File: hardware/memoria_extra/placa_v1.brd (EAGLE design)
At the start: 37.1 x 30.4 mm, 10 parts, among them IC1 CY7C1049CV33T, IC2 REG1117, J10 M14, J11 M14, J9 M14

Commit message: Actualizo esquemas para v4.1
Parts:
- removed IC1: CY7C1049CV33T, memory-sram:TSOPII-Z44
- removed J9: M14, SparkFun:1X14
- added J12: (no value), pinhead:1X12
- added U$1: (no value), GadgetFactory:TSOP44-II
- J10, J11: value M14 -> (none); device SparkFun:1X14 -> pinhead:1X12
- moved IC2 28.0 mm to (3.81, 5.33), flipped to the top
- moved C4 27.5 mm to (6.60, 12.2), flipped to the top, turned to 270 degrees
- moved C3 25.5 mm to (3.81, 12.2), flipped to the top, turned to 270 degrees
- moved J10 15.4 mm to (16.8, 21.3)
- moved C2 14.7 mm to (10.4, 2.54), flipped to the top
- moved J11 14.2 mm to (15.5, 18.8)
- moved C1 6.68 mm to (10.4, 12.2), flipped to the top, turned to 270 degrees
- moved L1 5.89 mm to (1.02, 12.7), flipped to the top
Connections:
- removed net M0: J9.13
- removed net M1: J10.13
- removed net M2: J11.13
- net /WE: now also U$1.15; no longer IC1.15, J11.4
- net 3.3V: now also J11.1, J12.12, U$1.11, U$1.33; no longer IC1.11, IC1.33
- net A0: now also U$1.3; no longer IC1.3, J9.7
- net A1: now also U$1.4; no longer IC1.4, J10.7
- net A10: now also U$1.26; no longer IC1.26, J10.12
- net A11: now also U$1.27; no longer IC1.27, J9.12
- net A12: now also U$1.28; no longer IC1.28, J11.11
- net A13: now also U$1.29; no longer IC1.29, J10.11
- net A14: now also U$1.30; no longer IC1.30, J9.11
- net A15: now also U$1.38; no longer IC1.38, J10.9
- net A16: now also U$1.39; no longer IC1.39, J11.9
- net A17: now also U$1.40; no longer IC1.40, J9.10
- net A18: now also U$1.41; no longer IC1.41, J10.10
- net A19: now also U$1.25; no longer J11.12
- net A2: now also U$1.5; no longer IC1.5, J11.7
- net A20: now also J10.1, U$1.42; no longer J11.10
- net A3: now also U$1.6; no longer IC1.6, J11.6
- net A4: now also U$1.7; no longer IC1.7, J10.6
- net A5: now also U$1.16; no longer IC1.16, J10.4
- net A6: now also U$1.17; no longer IC1.17, J9.4
- net A7: now also U$1.18; no longer IC1.18, J11.2
- net A8: now also U$1.19; no longer IC1.19, J10.2
- net A9: now also U$1.20; no longer IC1.20, J9.2
- net D0: now also U$1.9; no longer IC1.9, J9.6
- net D1: now also U$1.10; no longer IC1.10, J11.5
- net D2: now also U$1.13; no longer IC1.13, J10.5
- net D3: now also U$1.14; no longer IC1.14, J9.5
- net D4: now also U$1.31; no longer IC1.31, J9.8
- net D5: now also U$1.32; no longer IC1.32, J10.8
- net D6: now also U$1.35; no longer IC1.35, J11.8
- net D7: now also U$1.36; no longer IC1.36, J9.9
- net GND: now also J10.12, J11.12, U$1.12, U$1.34, U$1.37, U$1.8; no longer IC1.12, IC1.34, IC1.37, IC1.8, J10.1, J10.14
- net N$1: now also J12.1; no longer J11.1
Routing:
- net GND: track 88.0 -> 16.7 mm, vias 12 -> 0
- net +5V: track 46.7 -> 6.83 mm, vias 2 -> 0
- net A9: track 34.0 -> 0.00 mm, vias 1 -> 0
- net A8: track 30.3 -> 0.00 mm
- net A6: track 28.7 -> 0.00 mm, vias 1 -> 0
- net A11: track 26.6 -> 0.00 mm, vias 1 -> 0
- net D4: track 25.8 -> 0.00 mm, vias 1 -> 0
- net A7: track 25.1 -> 0.00 mm
- net A10: track 25.1 -> 0.00 mm
- net D3: track 25.0 -> 0.00 mm, vias 1 -> 0
- net A5: track 24.8 -> 0.00 mm
- net A14: track 23.7 -> 0.00 mm, vias 1 -> 0
- net A19: track 23.0 -> 0.00 mm
- net D5: track 22.5 -> 0.00 mm
- net A13: track 22.3 -> 0.00 mm
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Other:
- board size 37.1 x 30.4 mm -> 32.2 x 22.8 mm

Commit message: Finalizo placa
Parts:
- added SJ1: (no value), jumper:SJ_2
- moved J10 1.65 mm to (16.8, 23.0)
- moved J11 1.65 mm to (15.5, 20.4)
- moved J12 1.65 mm to (16.8, 17.9)
- moved C1 0.63 mm to (9.78, 12.2), turned to 90 degrees
- moved U$1 0.57 mm to (21.7, 7.37)
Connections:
- new net 3.3VIN: J11.1, J12.12, SJ1.3
- new net 3.3VREG: C4.1, IC2.2, SJ1.1
- net /WE: now also J11.5
- net 3.3V: now also SJ1.2; no longer C4.1, IC2.2, J11.1, J12.12
- net A0: now also J10.1
- net A1: now also J11.2
- net A10: now also J11.10
- net A11: now also J10.9
- net A12: now also J12.9
- net A13: now also J11.9
- net A14: now also J10.8
- net A15: now also J11.7
- net A16: now also J10.6
- net A17: now also J11.6
- net A18: now also J12.5
- net A19: now also J12.10
- net A2: now also J12.2
- net A20: now also J10.4; no longer J10.1
- net A3: now also J10.2
- net A4: now also J11.3
- net A5: now also J10.5
- net A6: now also J12.6
- net A7: now also J10.10
- net A8: now also J11.11
- net A9: now also J12.11
- net D0: now also J12.3
- net D1: now also J10.3
- net D2: now also J11.4
- net D3: now also J12.4
- net D4: now also J12.8
- net D5: now also J11.8
- net D6: now also J10.7
- net D7: now also J12.7
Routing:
- net 3.3VIN: track 0.00 -> 48.4 mm, vias 0 -> 1
- net GND: track 16.7 -> 52.6 mm, vias 0 -> 5
- net A0: track 0.00 -> 28.6 mm
- net A3: track 0.00 -> 28.1 mm
- net D1: track 0.00 -> 27.8 mm
- net A5: track 0.00 -> 26.5 mm
- net A1: track 0.00 -> 25.8 mm
- net D2: track 0.00 -> 25.6 mm
- net A4: track 0.00 -> 25.3 mm
- net /WE: track 0.00 -> 24.2 mm
- net 3.3VREG: track 0.00 -> 24.0 mm
- net A7: track 0.00 -> 23.6 mm
- net A2: track 0.00 -> 22.9 mm
- net D0: track 0.00 -> 22.7 mm
- net D3: track 0.00 -> 21.9 mm
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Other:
- board size 32.2 x 22.8 mm -> 32.2 x 24.4 mm

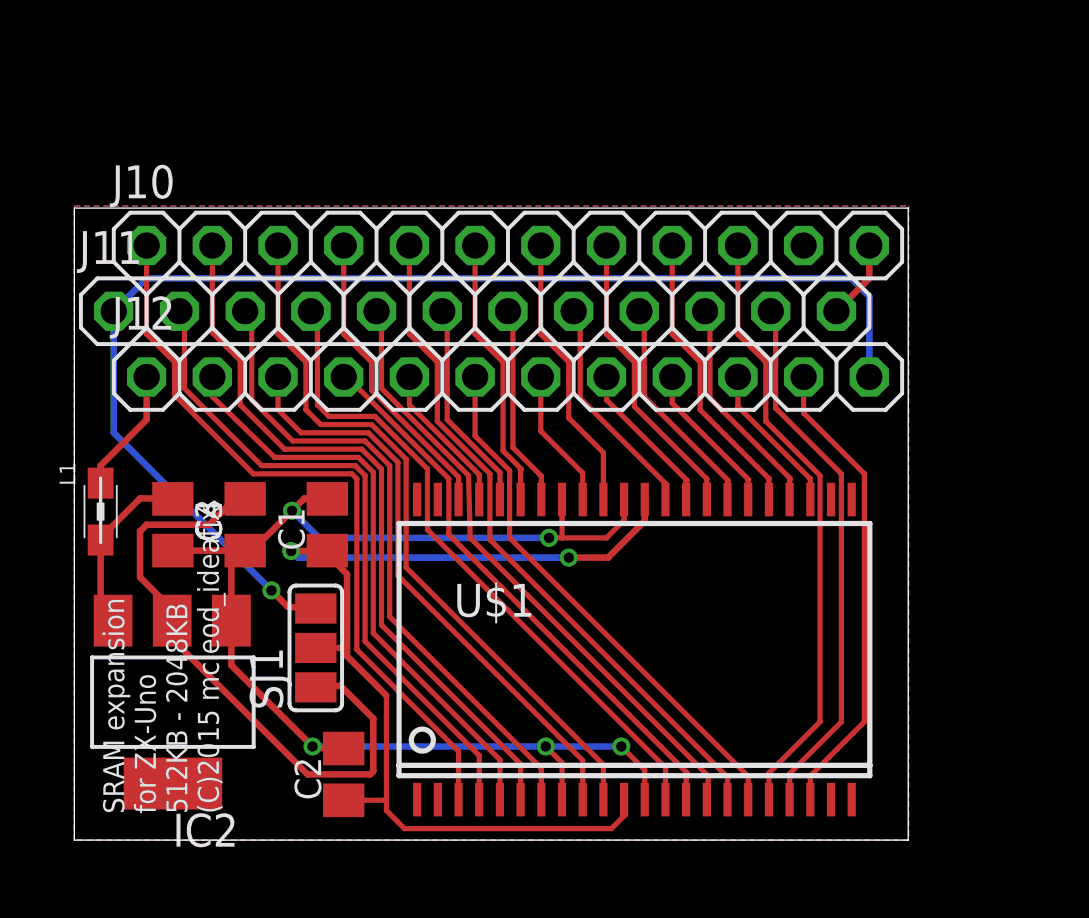
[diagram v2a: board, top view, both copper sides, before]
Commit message: Ajuste de espacio entre pads y mejora serigrafía
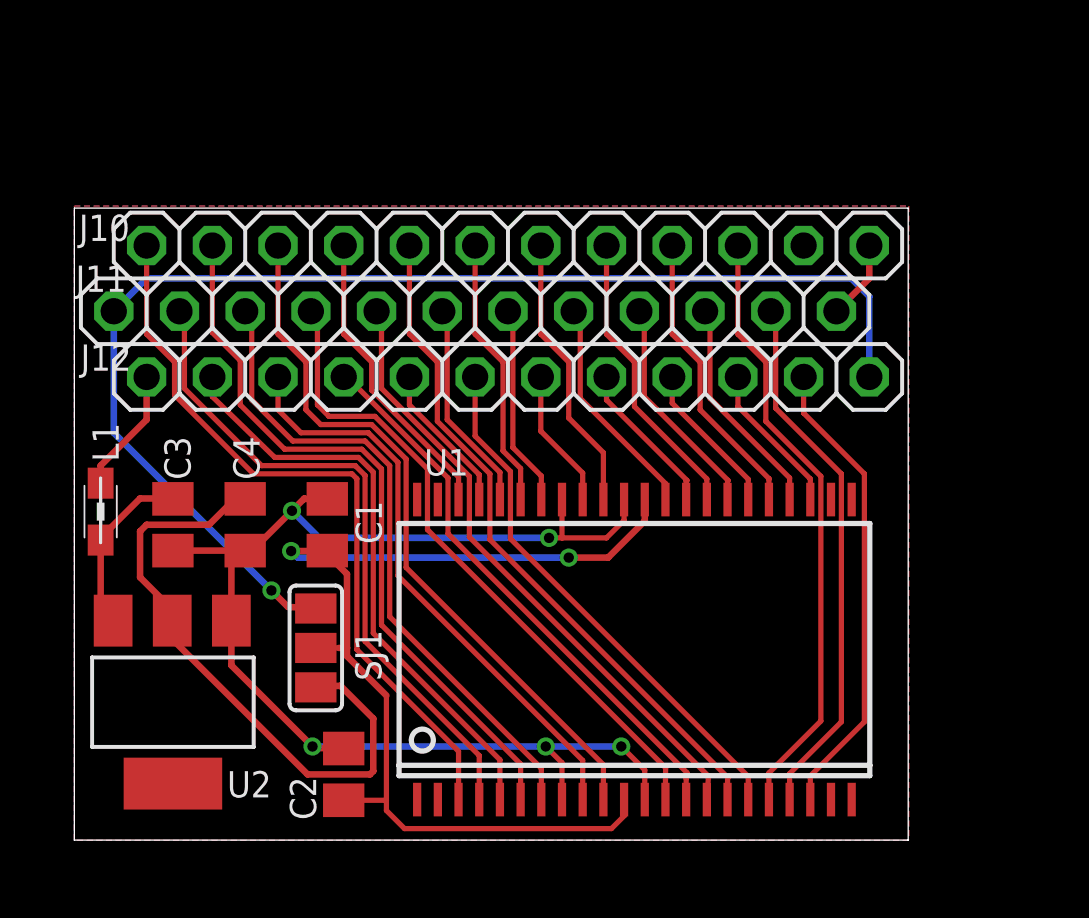
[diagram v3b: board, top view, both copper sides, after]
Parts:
- renumbered IC2 to U2, U$1 to U1
